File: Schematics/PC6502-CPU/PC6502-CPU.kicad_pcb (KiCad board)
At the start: 4 copper layers, 100 x 100 mm, 71 parts, among them J1 BUS, J2 CONSOLE, J4 TEST, J5 Conn_02x05_Odd_Even, J6 Conn_02x02_Odd_Even, U1 MC68B50, U2 628128_DIP32_SSOP32, U3 SST39SF010, U4 ATF1502AS, U5 W65C02, U6 74AHC244, U7 74LS161, X1 CXO_DIP8, X2 ASCO

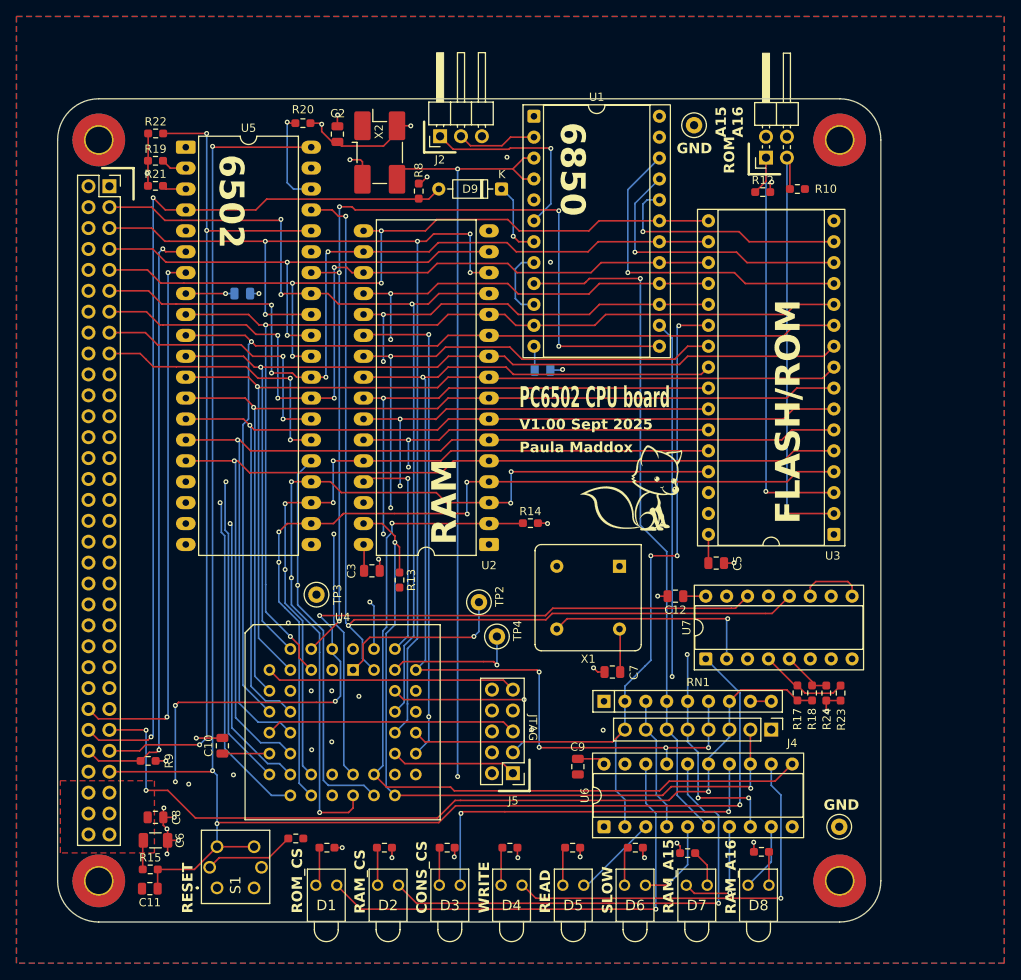
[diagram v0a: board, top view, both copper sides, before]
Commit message: Created V1.1 Schematic and PCB
A LOT of changes from v1.00;
removed clock stretcher (will now live in the CPLD)
moved the USB interface direct to the PCB
changed power pins
Added extra capacitance
Used Grant Searle's OSI basic and memory map to bring up the board
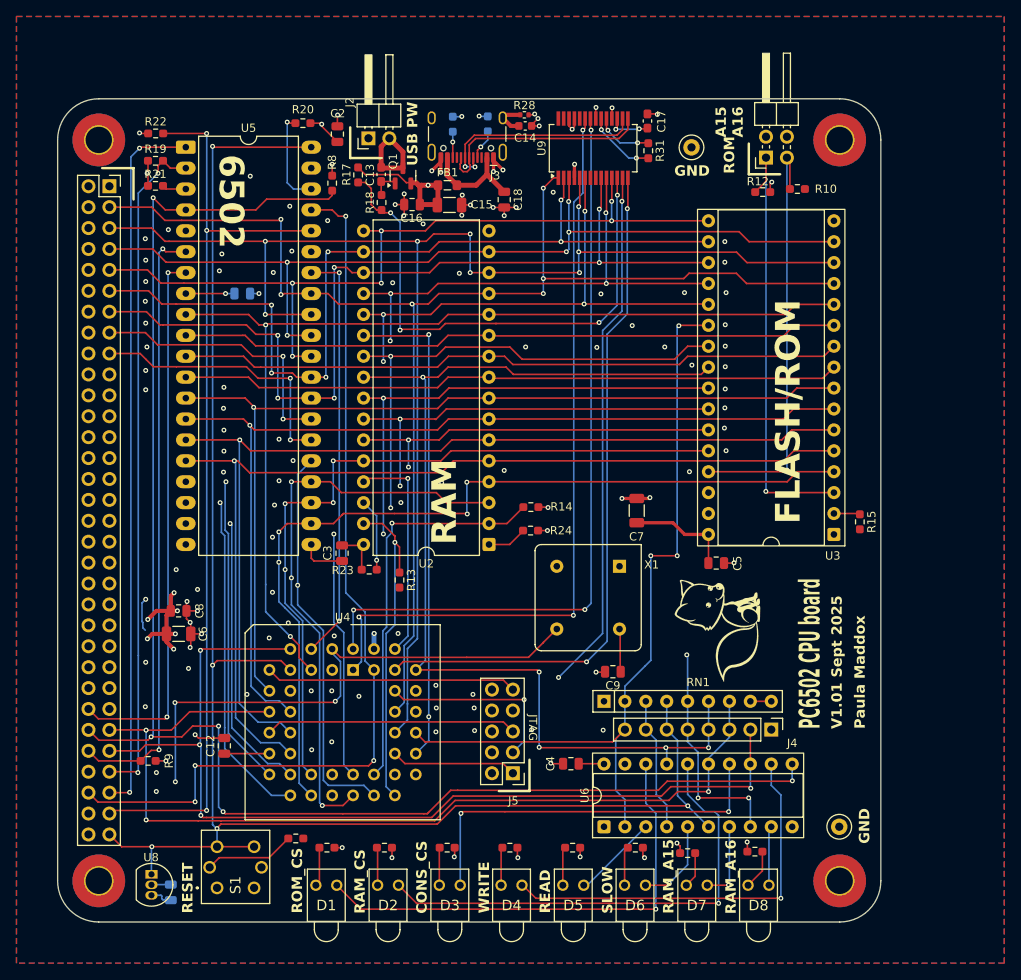
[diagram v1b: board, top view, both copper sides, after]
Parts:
- removed C10: 100nF, Capacitor_SMD:C_0805_2012Metric
- removed D9: 1N4148, Diode_THT:D_DO-35_SOD27_P7.62mm_Horizontal
- removed TP2, TP3, TP4: TestPoint, TestPoint:TestPoint_Loop_D1.80mm_Drill1.0mm_Beaded
- removed U1: MC68B50, Package_DIP:DIP-24_W15.24mm_Socket
- removed U7: 74LS161, Package_DIP:DIP-16_W7.62mm_Socket
- removed X2: ASCO, Oscillator:Oscillator_SMD_EuroQuartz_XO91-4Pin_7.0x5.0mm_HandSoldering
- added C13: 100nF, Capacitor_SMD:C_0603_1608Metric_Pad1.08x0.95mm_HandSolder, F.Cu at (139.3, 59.2)
- added C14: 100nF 100V, Capacitor_SMD:C_0603_1608Metric, F.Cu at (156.8, 53.3)
- added C15: 47uF, Capacitor_SMD:C_1206_3216Metric, F.Cu at (147.6, 62.9)
- added C16: 100nF, Capacitor_SMD:C_0805_2012Metric, F.Cu at (143.1, 62.9)
- added C17: 100nF, Capacitor_SMD:C_0603_1608Metric_Pad1.08x0.95mm_HandSolder, F.Cu at (171.7, 52.7)
- added C18: 100nF, Capacitor_SMD:C_0805_2012Metric, F.Cu at (154.2, 62.2)
- added FB1: FerriteBead_Small, Inductor_SMD:L_0805_2012Metric_Pad1.05x1.20mm_HandSolder, F.Cu at (147.3, 60.5)
- added J3: USB_C_Receptacle_USB2.0_16P, Connector_USB:USB_C_Receptacle_HCTL_HC-TYPE-C-16P-01A, F.Cu at (149.8, 53.4)
- added Q1: IRLML6402, Package_TO_SOT_SMD:SOT-23, F.Cu at (141.9, 59.4)
- added R28: 330R, Resistor_SMD:R_0402_1005Metric, F.Cu at (156.7, 52.0)
- added R29: 5K1, Resistor_SMD:R_0603_1608Metric_Pad0.98x0.95mm_HandSolder, B.Cu at (148.0, 53.1)
- added R30: 5K1, Resistor_SMD:R_0603_1608Metric_Pad0.98x0.95mm_HandSolder, B.Cu at (152.2, 53.0)
- added R31: 10k, Resistor_SMD:R_0603_1608Metric_Pad0.98x0.95mm_HandSolder, F.Cu at (171.8, 56.3)
- added U8: MCP130-450DI/TO, Package_TO_SOT_THT:TO-92_Inline, F.Cu at (111.4, 144.2)
- added U9: FT245RNL, Package_SO:SSOP-28_5.3x10.2mm_P0.65mm, F.Cu at (165.1, 56.0)
- C11: moved to B.Cu
- C4: moved to F.Cu
- C7: value 100nF -> 47uF; footprint Capacitor_SMD:C_0805_2012Metric -> Capacitor_SMD:C_1206_3216Metric
- J2: value CONSOLE -> Conn_01x02; footprint Connector_PinHeader_2.54mm:PinHeader_1x03_P2.54mm_Horizontal -> Connector_PinHeader_2.54mm:PinHeader_1x02_P2.54mm_Horizontal
- R15, R23, R24: value 4K7 -> 10K
- R17, R18: value 0R -> 10k
- U2: value 628128_DIP32_SSOP32 -> AS6C4008-55PCN; footprint Package_DIP:DIP-32_W15.24mm_LongPads -> Package_DIP:DIP-32_W15.24mm
- moved R15 96.0 mm to (197.4, 101.4), turned to -90 degrees
- moved R17 82.5 mm to (136.5, 59.2)
- moved R18 79.3 mm to (139.3, 62.6), turned to 90 degrees
- moved R23 59.2 mm to (137.8, 107.2), turned to 0 degrees
- moved C12 57.7 mm to (120.2, 128.6), turned to 90 degrees
- moved C4 47.9 mm to (162.3, 130.8), turned to 180 degrees
- moved R24 41.0 mm to (157.4, 102.5), turned to 0 degrees
- moved C8 25.2 mm to (114.7, 112.2)
- moved C6 25.2 mm to (114.7, 115.0)
- moved C7 19.8 mm to (170.3, 100.0), turned to 90 degrees
- moved FOX1 19.3 mm to (180.2, 113.9), turned to 90 degrees
- moved C9 12.3 mm to (167.4, 119.6), turned to 180 degrees
- moved R8 10.6 mm to (133.3, 60.2)
- moved J2 8.70 mm to (137.8, 54.8)
- moved C3 4.21 mm to (134.6, 105.2), turned to -90 degrees
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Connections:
- C11 pad 1: nRES -> GND
- C11 pad 2: GND -> +5V
- J1 pad 12: GND -> +5V
- J1 pad 16: GND -> +5V
- J1 pad 20: GND -> +5V
- J1 pad 24: GND -> +5V
- J1 pad 28: GND -> +5V
- J1 pad 32: GND -> +5V
- J1 pad 36: GND -> +5V
- J1 pad 4: GND -> +5V
- J1 pad 40: GND -> +5V
- J1 pad 44: GND -> +5V
- J1 pad 48: GND -> +5V
- J1 pad 53: nSLOW -> nSLOW0
- J1 pad 55: nBUSRQ -> nSLOW1
- J1 pad 57: nRES -> RDY
- J1 pad 58: CLK -> SYSCLK
- J1 pad 59: +5V -> nVP
- J1 pad 60: SPCLK -> CPU_CLK
- J1 pad 61: +5V -> nBUSRQ
- J1 pad 62: +5V -> unconnected-(J1-Pin_62-Pad62)
- J1 pad 63: +5V -> nRES
- J1 pad 64: +5V -> GND
- J1 pad 8: GND -> +5V
- J2 pad 1: Net-(J2-Pin_1) -> +5V
- J4 pad 2: RAM_A15 -> nSLOW1
- J4 pad 3: nSLOW -> nSLOW0
- J4 pad 6: nCONSOLE_CS -> nRES
- J6 pad 3: ROM_A16 -> ROM_A14
- R10 pad 1: ROM_A16 -> ROM_A14
- R15 pad 1: +5V -> Net-(U3-A16)
- R15 pad 2: nRES -> GND
- R17 pad 1: nSLOW -> Net-(U9-~{PWREN})
- R17 pad 2: Net-(U7-D1) -> /60FAKE50/VUSB
- R18 pad 1: Net-(U7-D2) -> Net-(U9-~{PWREN})
- R18 pad 2: nSLOW -> Net-(Q1-G)
- R19 pad 2: Net-(U5-RDY) -> RDY
- R23 pad 2: Net-(U7-D1) -> Net-(U2-A17)
- R24 pad 1: +5V -> Net-(U2-A18)
- R24 pad 2: Net-(U7-D2) -> GND
- R6 pad 1: Net-(D7-K) -> Net-(D7-A)
- R6 pad 2: GND -> +5V
- R7 pad 1: Net-(D8-K) -> Net-(D8-A)
- R7 pad 2: GND -> +5V
- RN1 pad 4: nCONSOLE_CS -> nRES
- RN1 pad 7: nSLOW -> nSLOW0
- U2 pad 1: unconnected-(U2-NC-Pad1) -> Net-(U2-A18)
- U2 pad 30: +5V -> Net-(U2-A17)
- U3 pad 2: ROM_A16 -> Net-(U3-A16)
- U3 pad 29: /A14 -> ROM_A14
- U4 pad 1: Net-(U4-I/GCLR) -> nRXF
- U4 pad 11: /A1 -> nSLOW0
- U4 pad 2: CLK -> SYSCLK
- U4 pad 29: nCONSOLE_CS -> RAM_A17
- U4 pad 37: 6850_E -> nRD_FT
- U4 pad 41: Net-(U4-I/O/GCLK3) -> nWR_FT
- U4 pad 44: Net-(U4-I/OE1) -> nTXE
- U4 pad 6: /A2 -> nSLOW1
- U4 pad 8: /A3 -> nRES
- U5 pad 1: unconnected-(U5-VPB-Pad1) -> nVP
- U5 pad 2: Net-(U5-RDY) -> RDY
- U6 pad 11: RAM_A16 -> nIRQ
- U6 pad 13: RAM_A15 -> nSLOW1
- U6 pad 15: nSLOW -> nSLOW0
- U6 pad 6: nCONSOLE_CS -> nRES
- U6 pad 7: Net-(D7-A) -> Net-(D7-K)
- U6 pad 9: Net-(D8-A) -> Net-(D8-K)
- X1 pad 5: PHI2x2 -> SYSCLK
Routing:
- net SPCLK: track 141.8 -> 0.00 mm, vias 2 -> 0
- net nSLOW1: track 0.00 -> 118.1 mm, vias 0 -> 4
- net nCONSOLE_CS: track 115.9 -> 0.00 mm, vias 1 -> 0
- net nSLOW0: track 0.00 -> 113.1 mm, vias 0 -> 3
- net nSLOW: track 106.0 -> 0.00 mm, vias 3 -> 0
- net CLK: track 104.7 -> 0.00 mm, vias 4 -> 0
- net nRXF: track 0.00 -> 94.0 mm, vias 0 -> 3
- net nTXE: track 0.00 -> 92.9 mm, vias 0 -> 3
- net nVP: track 0.00 -> 86.9 mm, vias 0 -> 2
- net nWR_FT: track 0.00 -> 84.6 mm, vias 0 -> 2
- net RDY: track 0.00 -> 82.2 mm, vias 0 -> 2
- net nRD_FT: track 0.00 -> 81.9 mm, vias 0 -> 2
- net nIRQ: track 110.2 -> 189.9 mm, vias 2 -> 5
- net SYSCLK: track 0.00 -> 76.4 mm, vias 0 -> 3
- net 6850_E: track 75.2 -> 0.00 mm, vias 1 -> 0
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- removed copper zone on F.Cu, net +5V
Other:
- board text added: "USB PW"
- board text added: "V1.01 Sept 2025"
- board text removed: "6850"
- board text removed: "V1.00 Sept 2025"

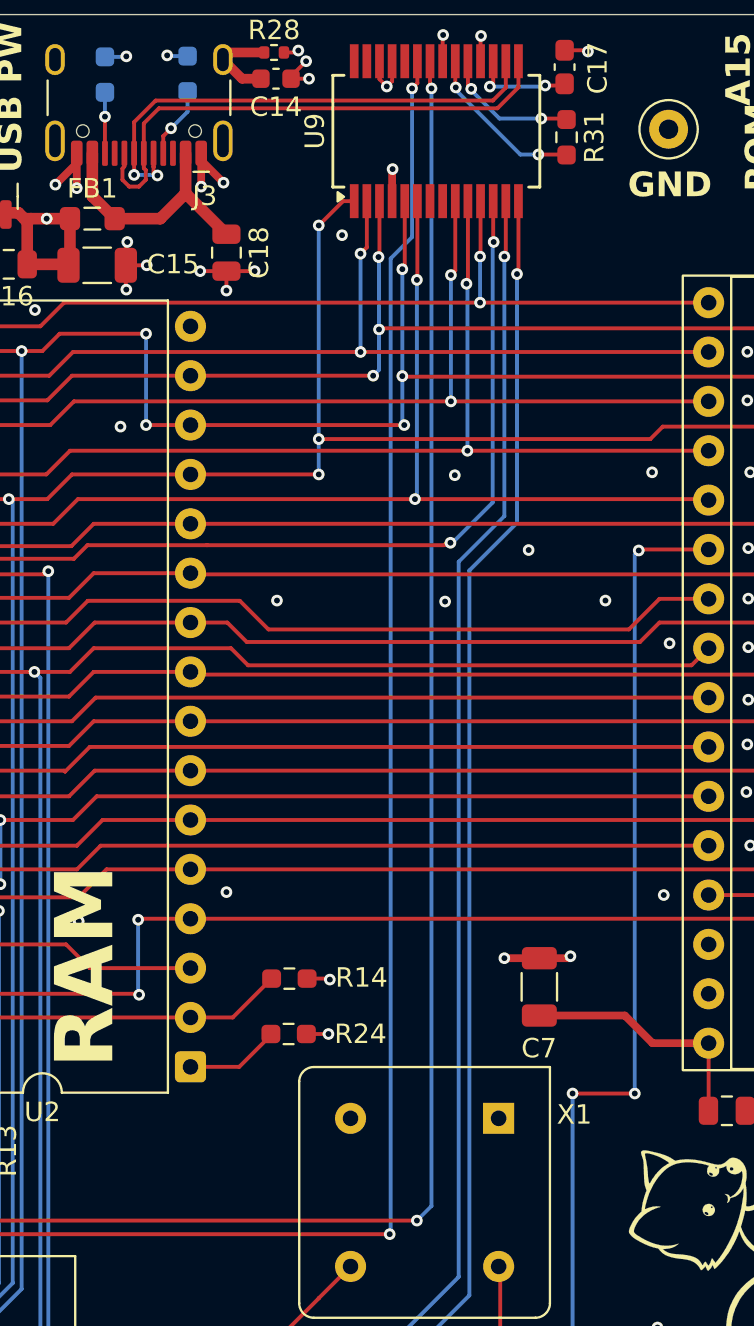
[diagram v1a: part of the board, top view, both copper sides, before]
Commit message: FT245 WRITE signal correction
I had it marked as active low when it's active high, updated.
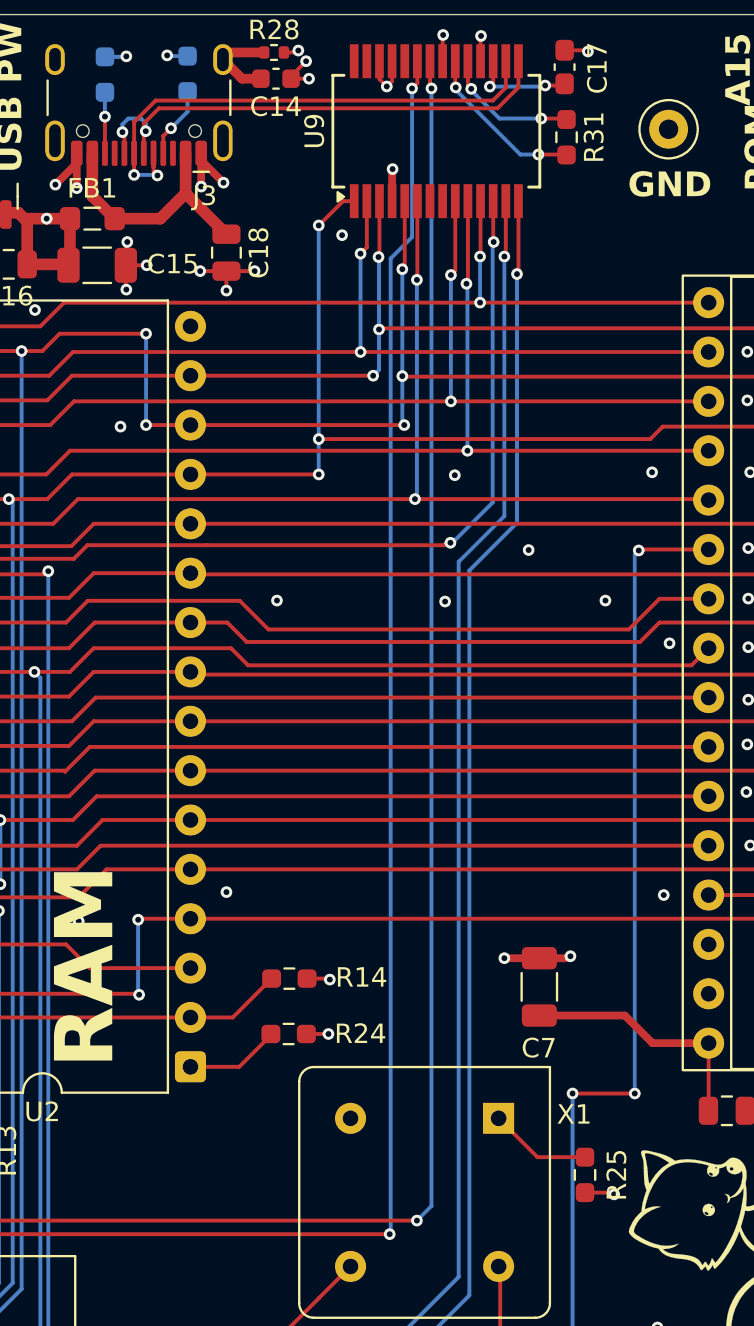
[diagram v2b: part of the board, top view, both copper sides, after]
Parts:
- added R25: 3K3, Resistor_SMD:R_0603_1608Metric_Pad0.98x0.95mm_HandSolder, F.Cu at (172.7, 109.7)
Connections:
- X1 pad 1: unconnected-(X1-EN-Pad1) -> Net-(X1-EN)
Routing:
- net Net-(X1-EN): track 0.00 -> 5.27 mm
- net +5V: track 77.1 -> 78.6 mm, vias 20 -> 21
- net /60FAKE50/USB_D+: track 26.9 -> 25.9 mm, vias 0 -> 2

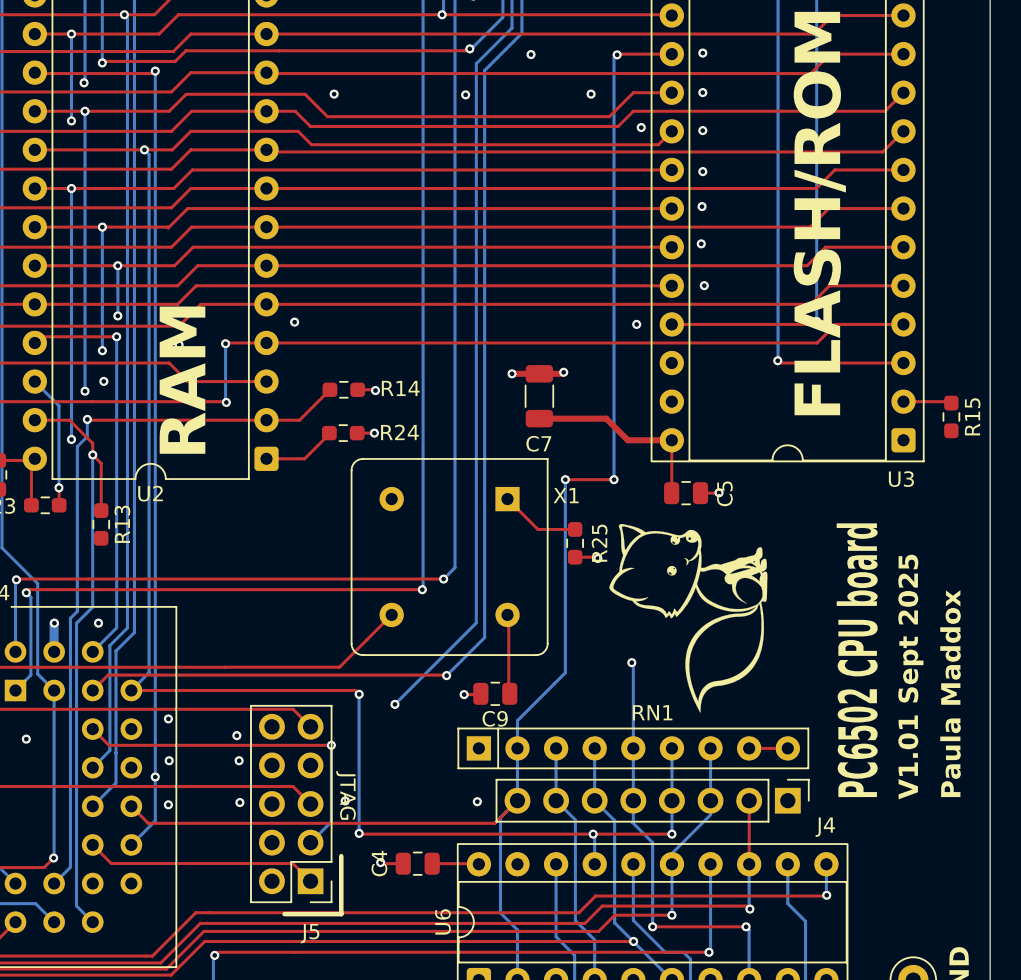
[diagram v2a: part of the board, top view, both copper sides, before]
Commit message: V1.1 CPU, VIA and POWER PCBs uploaded
A simpler CPU board (direct link to FT245R, 74161 removed and some tidying of tracks). Fixed a couple of floating inputs to RAM/ROM
VIA is much simpler, having just the one VIA chip.
POWER board has USB-PD and a 24VDC input for higher power stuff in the future.
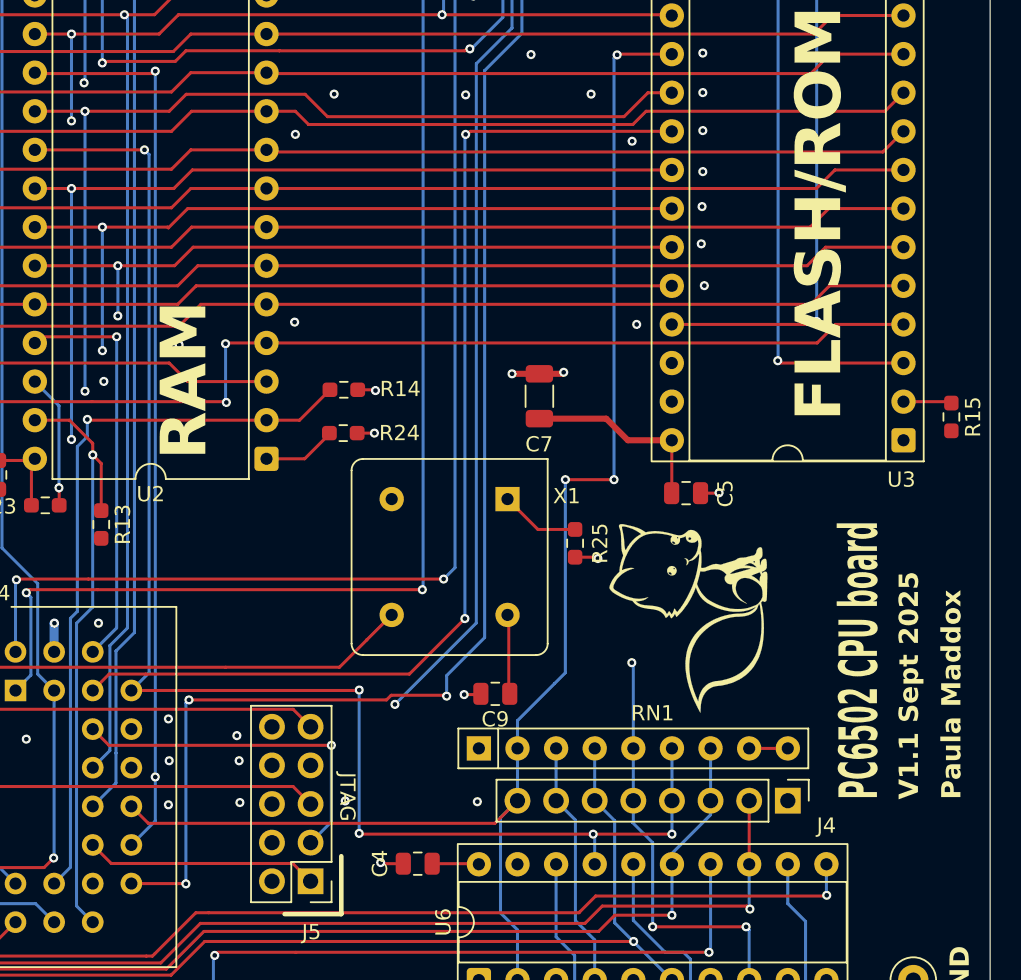
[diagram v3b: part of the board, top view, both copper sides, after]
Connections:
- U3 pad 24: nR -> ROM_nR
- U4 pad 29: RAM_A17 -> WR_FT
- U4 pad 41: nWR_FT -> ROM_nR
- U9 pad 14: nWR_FT -> WR_FT
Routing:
- net WR_FT: track 0.00 -> 95.1 mm, vias 0 -> 4
- net nWR_FT: track 84.6 -> 0.00 mm, vias 2 -> 0
- net ROM_nR: track 0.00 -> 72.0 mm, vias 0 -> 2
- net nR: track 131.8 -> 96.1 mm
- net GND: vias 117 -> 118
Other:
- board text added: "V1.1 Sept 2025"
- board text removed: "V1.01 Sept 2025"
